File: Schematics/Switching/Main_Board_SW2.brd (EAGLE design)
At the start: 99.9 x 80 mm, 85 parts, among them IC3 SWITCHER, IC4 SWITCHER, Q1 32.768kHz, X1 MINI-USB-SHIELD-UX60-MB-5ST, X2 RJ45

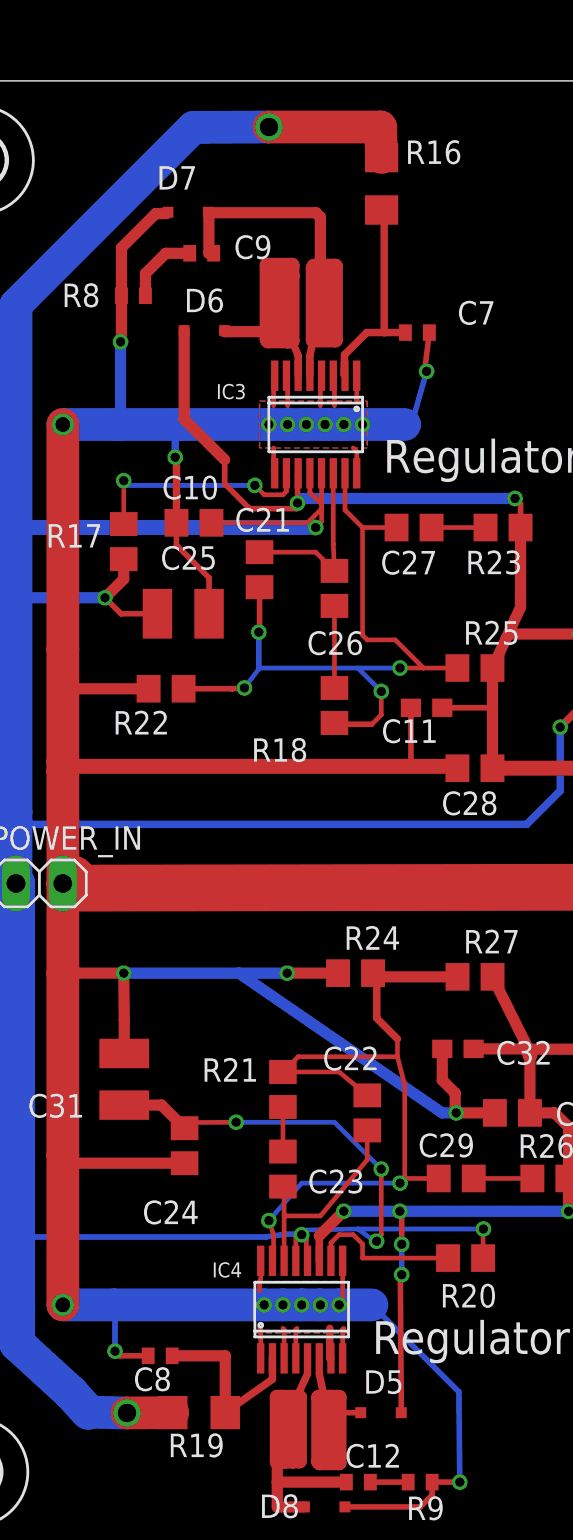
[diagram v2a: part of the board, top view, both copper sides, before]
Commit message: PCB Verified. Add Battery Sense
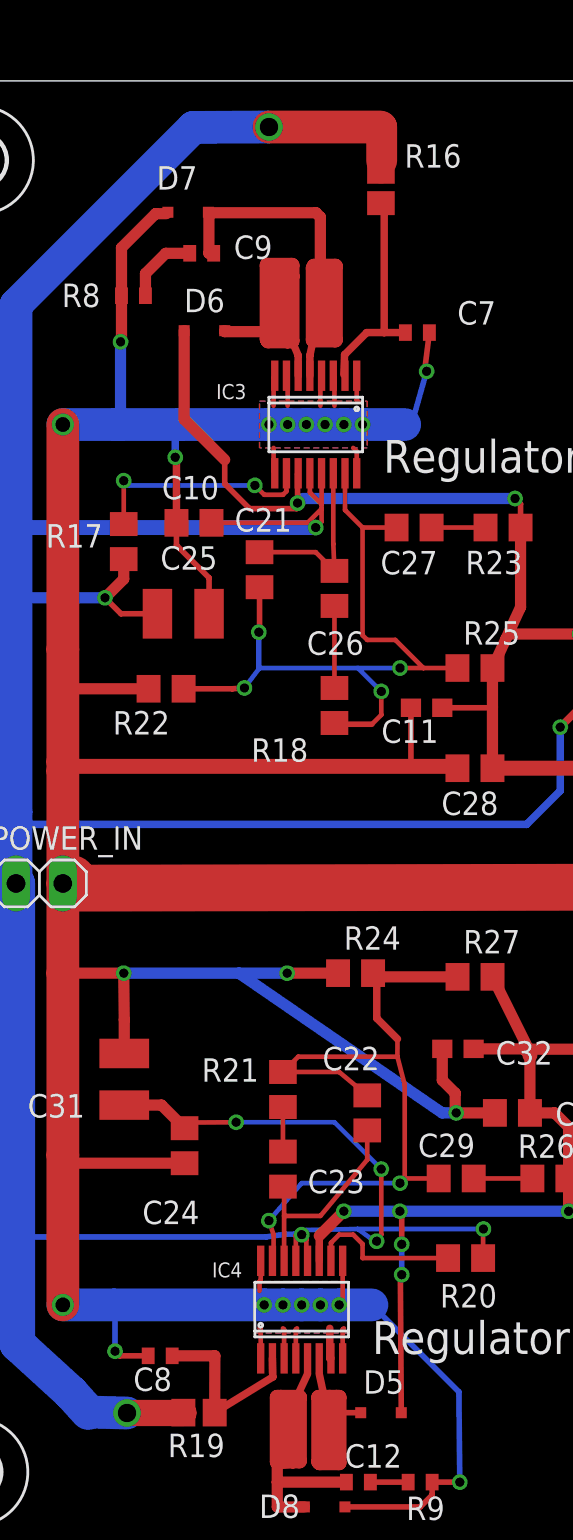
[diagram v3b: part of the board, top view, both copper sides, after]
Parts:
- R16, R19: device resistor:R1206 -> resistor:R0805
- moved R16 0.20 mm to (26.3, 74.2)
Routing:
- net V+: track 236.1 -> 237.5 mm
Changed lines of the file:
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@@
 <setting verticaltext="up"/>
 </settings>
-<grid distance="0.025" unitdist="mm" unit="mm" style="lines" multiple="1" display="yes" altdistance="0.025" altunitdist="mm" altunit="mm"/>
+<grid distance="0.0125" unitdist="mm" unit="mm" style="lines" multiple="1" display="yes" altdistance="0.0125" altunitdist="mm" altunit="mm"/>
 <layers>
 <layer number="1" name="Top" color="4" fill="1" visible="yes" active="yes"/>
@@
 <layer number="25" name="tNames" color="7" fill="1" visible="yes" active="yes"/>
 <layer number="26" name="bNames" color="7" fill="1" visible="yes" active="yes"/>
-<layer number="27" name="tValues" color="7" fill="1" visible="yes" active="yes"/>
-<layer number="28" name="bValues" color="7" fill="1" visible="yes" active="yes"/>
+<layer number="27" name="tValues" color="7" fill="1" visible="no" active="yes"/>
+<layer number="28" name="bValues" color="7" fill="1" visible="no" active="yes"/>
 <layer number="29" name="tStop" color="7" fill="3" visible="yes" active="yes"/>
 <layer number="30" name="bStop" color="7" fill="6" visible="yes" active="yes"/>
@@
 <attribute name="VALUE" x="32.0085" y="62.2785" size="0.8128" layer="27" font="vector" rot="R180"/>
 </element>
-<element name="R16" library="resistor" package="R1206" value="499K" x="26.36" y="74.372" smashed="yes" rot="R90">
-<attribute name="NAME" x="30.725" y="76.717" size="1.27" layer="25" rot="R180"/>
-<attribute name="VALUE" x="31.575" y="75.323" size="1.27" layer="27" rot="R180"/>
+<element name="R16" library="resistor" package="R0805" value="499K" x="26.3225" y="74.172" smashed="yes" rot="R90">
+<attribute name="NAME" x="30.6875" y="76.517" size="1.27" layer="25" rot="R180"/>
+<attribute name="VALUE" x="31.5375" y="75.123" size="1.27" layer="27" rot="R180"/>
 </element>
 <element name="R17" library="rcl" package="R0805" value="10k" x="12.372" y="54.964" smashed="yes" rot="R270">
@@
 <attribute name="VALUE" x="24.8815" y="15.5305" size="0.8128" layer="27" font="vector" rot="R270"/>
 </element>
-<element name="R19" library="resistor" package="R1206" value="499k" x="16.456" y="7.72" smashed="yes" rot="R180">
+<element name="R19" library="resistor" package="R0805" value="499k" x="16.456" y="7.72" smashed="yes" rot="R180">
 <attribute name="NAME" x="17.853" y="6.577" size="1.27" layer="25" rot="R180"/>
 <attribute name="VALUE" x="17.853" y="10.133" size="1.27" layer="27" rot="R180"/>
@@
 <wire x1="6.6" y1="11.45" x2="9.5" y2="8.8" width="1.9304" layer="16"/>
 <wire x1="6.53" y1="67.808" x2="16.15" y2="77.428" width="1.778" layer="16"/>
-<wire x1="26.3" y1="77.45" x2="26.36" y2="75.794" width="1.778" layer="1"/>
 <via x="12.55" y="7.7" extent="1-16" drill="1"/>
-<wire x1="15.034" y1="7.72" x2="12.55" y2="7.7" width="1.778" layer="1"/>
 <wire x1="12.55" y1="7.7" x2="10.45" y2="7.75" width="1.778" layer="16"/>
 <wire x1="16.15" y1="77.428" x2="20.25" y2="77.45" width="1.778" layer="16"/>
@@
 <wire x1="34.225" y1="39.625" x2="6.63" y2="39.625" width="0.4064" layer="16"/>
 <wire x1="6.63" y1="39.625" x2="6.53" y2="39.725" width="0.4064" layer="16"/>
+<wire x1="26.3" y1="77.45" x2="26.3625" y2="77.45" width="1.6764" layer="1"/>
+<wire x1="26.3625" y1="77.45" x2="26.3625" y2="75.6125" width="1.6764" layer="1"/>
+<wire x1="26.3625" y1="75.6125" x2="26.3225" y2="75.6125" width="1.27" layer="1"/>
+<wire x1="26.3225" y1="75.6125" x2="26.3225" y2="75.022" width="1.27" layer="1"/>
+<wire x1="12.55" y1="7.7" x2="15.606" y2="7.7" width="1.4224" layer="1"/>
+<wire x1="15.606" y1="7.7" x2="15.606" y2="7.72" width="1.4224" layer="1"/>
 </signal>
 <signal name="N$13">
@@
 <wire x1="25.55" y1="66.3" x2="26.5" y2="66.3" width="0.4064" layer="1"/>
 <wire x1="26.5" y1="66.3" x2="27.65" y2="66.3" width="0.4064" layer="1"/>
-<wire x1="26.36" y1="72.95" x2="26.5" y2="72.81" width="0.4064" layer="1"/>
+<wire x1="26.3225" y1="73.322" x2="26.5" y2="72.81" width="0.4064" layer="1"/>
 <wire x1="26.5" y1="72.81" x2="26.5" y2="66.3" width="0.4064" layer="1"/>
 </signal>
@@
 <contactref element="R19" pad="1"/>
 <contactref element="C8" pad="1"/>
-<wire x1="15" y1="10.8" x2="17.878" y2="10.8" width="0.6096" layer="1"/>
-<wire x1="17.878" y1="10.8" x2="17.878" y2="7.72" width="0.6096" layer="1"/>
-<wire x1="20.4365" y1="10.6622" x2="20.4365" y2="9.5285" width="0.4064" layer="1"/>
-<wire x1="20.4365" y1="9.5285" x2="17.878" y2="7.72" width="0.4064" layer="1"/>
+<wire x1="15" y1="10.8" x2="17.3155" y2="10.8" width="0.6096" layer="1"/>
+<wire x1="17.3155" y1="10.8" x2="17.306" y2="7.72" width="0.6096" layer="1"/>
+<wire x1="20.4365" y1="10.6622" x2="20.4615" y2="9.6535" width="0.4064" layer="1"/>
+<wire x1="20.4615" y1="9.6535" x2="17.306" y2="7.72" width="0.4064" layer="1"/>
 </signal>
 <signal name="N$33">

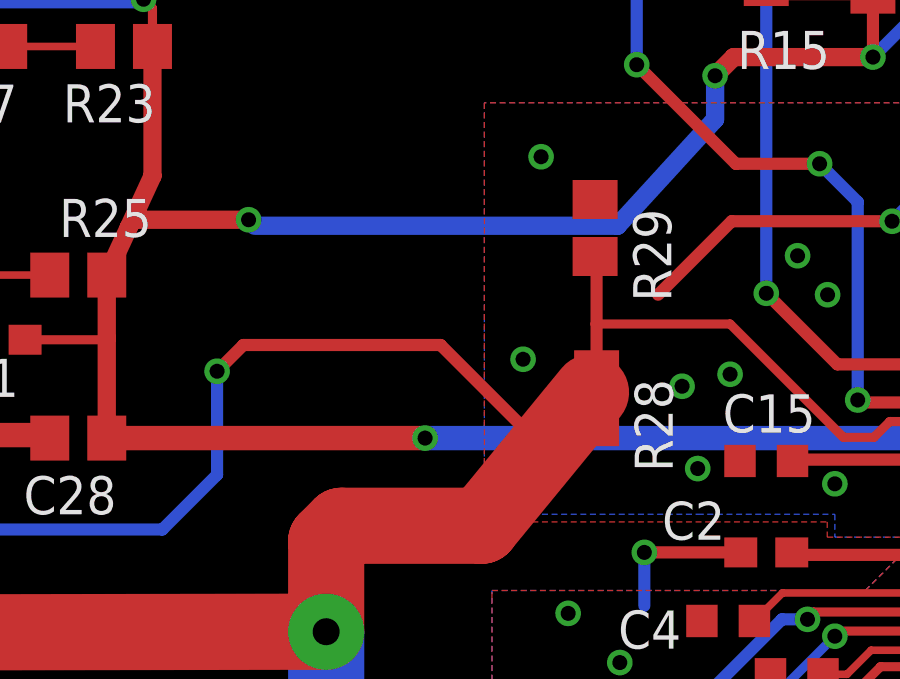
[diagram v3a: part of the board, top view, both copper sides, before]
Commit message: Batter Sense
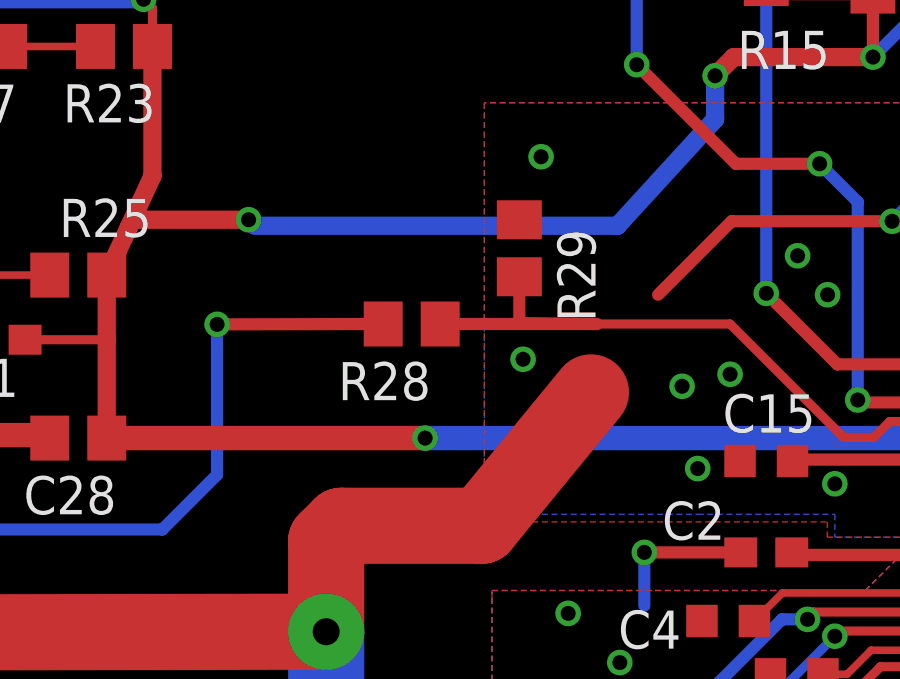
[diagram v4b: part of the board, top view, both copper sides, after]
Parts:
- moved R28 6.64 mm to (42.5, 46.5), turned to 180 degrees
- moved R29 2.61 mm to (46.1, 49.0)
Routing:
- net V+: track 237.5 -> 230.5 mm
- net N$22: track 16.5 -> 22.1 mm
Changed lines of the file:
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@@
 <element name="H3" library="holes" package="2,8" value="MOUNT-HOLE2.8" x="95.6" y="75.85"/>
 <element name="H4" library="holes" package="2,8" value="MOUNT-HOLE2.8" x="4.55" y="75.65"/>
-<element name="R28" library="rcl" package="R0805" value="5.6k" x="48.7" y="44" rot="R270"/>
-<element name="R29" library="rcl" package="R0805" value="5.6k" x="48.65" y="49.675" rot="R270"/>
+<element name="R28" library="rcl" package="R0805" value="5.6k" x="42.5375" y="46.475" rot="R180"/>
+<element name="R29" library="rcl" package="R0805" value="5.6k" x="46.125" y="49" rot="R270"/>
 </elements>
 <signals>
@@
 <wire x1="12.2" y1="61.564" x2="11.95" y2="61.314" width="0.6096" layer="16"/>
 <contactref element="R29" pad="1"/>
-<wire x1="61.214" y1="40.386" x2="61.42355" y2="38.14445" width="0" layer="19" extent="1-1"/>
 </signal>
 <signal name="N$11">
@@
 <wire x1="20.25" y1="77.45" x2="26.3" y2="77.45" width="1.778" layer="1"/>
 <contactref element="R28" pad="2"/>
-<wire x1="48.7" y1="43.05" x2="46.225" y2="43.05" width="0.4064" layer="1"/>
-<wire x1="46.225" y1="43.05" x2="43.5" y2="45.775" width="0.4064" layer="1"/>
-<wire x1="43.5" y1="45.775" x2="36.925" y2="45.775" width="0.4064" layer="1"/>
-<wire x1="36.925" y1="45.775" x2="36.05" y2="44.9" width="0.4064" layer="1"/>
 <wire x1="7.005" y1="39.825" x2="6.53" y2="40.3" width="0.4064" layer="16"/>
-<via x="36.05" y="44.9" extent="1-16" drill="0.5" diameter="0.254" shape="octagon"/>
-<wire x1="36.05" y1="44.9" x2="36.05" y2="41.45" width="0.4064" layer="16"/>
+<via x="36.05" y="46.4625" extent="1-16" drill="0.5" diameter="0.254" shape="octagon"/>
+<wire x1="36.05" y1="46.4625" x2="36.05" y2="41.45" width="0.4064" layer="16"/>
 <wire x1="36.05" y1="41.45" x2="34.225" y2="39.625" width="0.4064" layer="16"/>
 <wire x1="34.225" y1="39.625" x2="6.63" y2="39.625" width="0.4064" layer="16"/>
@@
 <wire x1="12.55" y1="7.7" x2="15.606" y2="7.7" width="1.4224" layer="1"/>
 <wire x1="15.606" y1="7.7" x2="15.606" y2="7.72" width="1.4224" layer="1"/>
+<wire x1="36.05" y1="46.4625" x2="41.5875" y2="46.475" width="0.4064" layer="1"/>
 </signal>
 <signal name="N$13">
@@
 <contactref element="R29" pad="2"/>
 <contactref element="R28" pad="1"/>
-<wire x1="48.7" y1="44.95" x2="48.7" y2="46.475" width="0.4064" layer="1"/>
-<wire x1="48.7" y1="46.475" x2="48.7" y2="48.675" width="0.4064" layer="1"/>
-<wire x1="48.7" y1="48.675" x2="48.65" y2="48.725" width="0.4064" layer="1"/>
+<wire x1="43.4875" y1="46.475" x2="48.7" y2="46.475" width="0.4064" layer="1"/>
+<wire x1="48.7" y1="46.475" x2="46.125" y2="46.5" width="0.4064" layer="1"/>
+<wire x1="46.125" y1="46.5" x2="46.125" y2="48.05" width="0.4064" layer="1"/>
 <contactref element="U$1" pad="P$44"/>
 <wire x1="59.65063125" y1="43.22445" x2="58.47445" y2="43.22445" width="0.3048" layer="1"/>

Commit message: Last layout sync of night
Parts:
- L1: value 4.7uH -> 3.3uH
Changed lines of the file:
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@@
 <?xml version="1.0" encoding="utf-8"?>
 <!DOCTYPE eagle SYSTEM "eagle.dtd">
-<eagle version="6.3">
+<eagle version="6.4">
 <drawing>
 <settings>
@@
 <layer number="26" name="bNames" color="7" fill="1" visible="yes" active="yes"/>
 <layer number="27" name="tValues" color="7" fill="1" visible="no" active="yes"/>
-<layer number="28" name="bValues" color="7" fill="1" visible="no" active="yes"/>
-<layer number="29" name="tStop" color="7" fill="3" visible="yes" active="yes"/>
-<layer number="30" name="bStop" color="7" fill="6" visible="yes" active="yes"/>
-<layer number="31" name="tCream" color="7" fill="4" visible="yes" active="yes"/>
-<layer number="32" name="bCream" color="7" fill="5" visible="yes" active="yes"/>
-<layer number="33" name="tFinish" color="6" fill="3" visible="yes" active="yes"/>
-<layer number="34" name="bFinish" color="6" fill="6" visible="yes" active="yes"/>
-<layer number="35" name="tGlue" color="7" fill="4" visible="yes" active="yes"/>
-<layer number="36" name="bGlue" color="7" fill="5" visible="yes" active="yes"/>
-<layer number="37" name="tTest" color="7" fill="1" visible="yes" active="yes"/>
-<layer number="38" name="bTest" color="7" fill="1" visible="yes" active="yes"/>
+<layer number="28" name="bValues" color="7" fill="1" visible="yes" active="yes"/>
+<layer number="29" name="tStop" color="7" fill="3" visible="no" active="yes"/>
+<layer number="30" name="bStop" color="7" fill="6" visible="no" active="yes"/>
+<layer number="31" name="tCream" color="7" fill="4" visible="no" active="yes"/>
+<layer number="32" name="bCream" color="7" fill="5" visible="no" active="yes"/>
+<layer number="33" name="tFinish" color="6" fill="3" visible="no" active="yes"/>
+<layer number="34" name="bFinish" color="6" fill="6" visible="no" active="yes"/>
+<layer number="35" name="tGlue" color="7" fill="4" visible="no" active="yes"/>
+<layer number="36" name="bGlue" color="7" fill="5" visible="no" active="yes"/>
+<layer number="37" name="tTest" color="7" fill="1" visible="no" active="yes"/>
+<layer number="38" name="bTest" color="7" fill="1" visible="no" active="yes"/>
 <layer number="39" name="tKeepout" color="4" fill="11" visible="yes" active="yes"/>
 <layer number="40" name="bKeepout" color="1" fill="11" visible="yes" active="yes"/>
@@
 <layer number="42" name="bRestrict" color="1" fill="10" visible="yes" active="yes"/>
 <layer number="43" name="vRestrict" color="2" fill="10" visible="yes" active="yes"/>
-<layer number="44" name="Drills" color="7" fill="1" visible="yes" active="yes"/>
-<layer number="45" name="Holes" color="7" fill="1" visible="yes" active="yes"/>
-<layer number="46" name="Milling" color="3" fill="1" visible="yes" active="yes"/>
-<layer number="47" name="Measures" color="7" fill="1" visible="yes" active="yes"/>
+<layer number="44" name="Drills" color="7" fill="1" visible="no" active="yes"/>
+<layer number="45" name="Holes" color="7" fill="1" visible="no" active="yes"/>
+<layer number="46" name="Milling" color="3" fill="1" visible="no" active="yes"/>
+<layer number="47" name="Measures" color="7" fill="1" visible="no" active="yes"/>
 <layer number="48" name="Document" color="7" fill="1" visible="yes" active="yes"/>
 <layer number="49" name="Reference" color="7" fill="1" visible="yes" active="yes"/>
 <layer number="50" name="dxf" color="7" fill="1" visible="no" active="no"/>
 <layer number="51" name="tDocu" color="7" fill="1" visible="yes" active="yes"/>
-<layer number="52" name="bDocu" color="7" fill="1" visible="yes" active="yes"/>
+<layer number="52" name="bDocu" color="7" fill="1" visible="no" active="yes"/>
 <layer number="53" name="tGND_GNDA" color="7" fill="1" visible="no" active="no"/>
 <layer number="54" name="bGND_GNDA" color="7" fill="1" visible="no" active="no"/>
@@
 <layer number="99" name="SpiceOrder" color="5" fill="1" visible="no" active="no"/>
 <layer number="100" name="Mechanical" color="7" fill="1" visible="no" active="no"/>
-<layer number="101" name="Gehäuse" color="7" fill="1" visible="yes" active="yes"/>
-<layer number="102" name="Mittellin" color="7" fill="1" visible="yes" active="yes"/>
-<layer number="103" name="Stiffner" color="7" fill="1" visible="yes" active="yes"/>
-<layer number="104" name="Name" color="7" fill="1" visible="yes" active="yes"/>
+<layer number="101" name="Gehäuse" color="7" fill="1" visible="no" active="yes"/>
+<layer number="102" name="Mittellin" color="7" fill="1" visible="no" active="yes"/>
+<layer number="103" name="Stiffner" color="7" fill="1" visible="no" active="yes"/>
+<layer number="104" name="Name" color="7" fill="1" visible="no" active="yes"/>
 <layer number="105" name="Beschreib" color="9" fill="1" visible="no" active="no"/>
 <layer number="106" name="BGA-Top" color="4" fill="1" visible="no" active="no"/>
@@
 <layer number="114" name="Route14" color="7" fill="1" visible="no" active="no"/>
 <layer number="115" name="Route15" color="7" fill="1" visible="no" active="no"/>
-<layer number="116" name="Patch_BOT" color="7" fill="1" visible="yes" active="yes"/>
+<layer number="116" name="Patch_BOT" color="7" fill="1" visible="no" active="yes"/>
 <layer number="117" name="mPads" color="7" fill="1" visible="no" active="no"/>
 <layer number="118" name="mVias" color="7" fill="1" visible="no" active="no"/>
@@
 <layer number="148" name="mDocument" color="7" fill="1" visible="no" active="no"/>
 <layer number="149" name="mReference" color="7" fill="1" visible="no" active="no"/>
-<layer number="150" name="Notes" color="7" fill="1" visible="yes" active="yes"/>
+<layer number="150" name="Notes" color="7" fill="1" visible="no" active="yes"/>
 <layer number="151" name="HeatSink" color="14" fill="1" visible="no" active="no"/>
 <layer number="152" name="mbDocu" color="7" fill="1" visible="no" active="no"/>
@@
 <layer number="195" name="mNames" color="7" fill="1" visible="no" active="no"/>
 <layer number="196" name="mValues" color="7" fill="1" visible="no" active="no"/>
-<layer number="199" name="EXTD_ERC" color="7" fill="1" visible="yes" active="yes"/>
+<layer number="199" name="EXTD_ERC" color="7" fill="1" visible="no" active="yes"/>
 <layer number="200" name="200bmp" color="1" fill="10" visible="no" active="no"/>
 <layer number="201" name="201bmp" color="2" fill="1" visible="no" active="no"/>
 <layer number="202" name="202bmp" color="3" fill="1" visible="no" active="no"/>
-<layer number="216" name="SMD16" color="7" fill="1" visible="yes" active="yes"/>
+<layer number="216" name="SMD16" color="7" fill="1" visible="no" active="yes"/>
 <layer number="231" name="Eagle3D_PG1" color="14" fill="1" visible="yes" active="yes"/>
 <layer number="232" name="Eagle3D_PG2" color="14" fill="2" visible="yes" active="yes"/>
@@
 </polygon>
 <text x="91.9" y="34.1" size="1.778" layer="25">USB</text>
-<text x="42.35" y="70.3" size="1.778" layer="25">Ethernet</text>
-<text x="52.55" y="27.8" size="1.778" layer="25">Microcontroller</text>
+<text x="44.8875" y="62.0875" size="1.778" layer="25">Ethernet</text>
+<text x="46.725" y="26.825" size="1.778" layer="25">Microcontroller</text>
 <text x="68" y="14.05" size="1.778" layer="25">Programmer</text>
 <text x="26.45" y="58.7" size="1.778" layer="25">Regulator 5V</text>
@@
 <attribute name="VALUE" x="8.301" y="52.932" size="1.27" layer="27"/>
 </element>
-<element name="L1" library="Inductor" package="SHEILDED_COIL" value="4.7uH" x="23.29" y="66.61" smashed="yes">
-<attribute name="VALUE" x="20.965" y="65.86" size="0.227" layer="48"/>
-<attribute name="NAME" x="20.75" y="69.375" size="0.227" layer="48"/>
+<element name="L1" library="Inductor" package="SHEILDED_COIL" value="3.3uH" x="23.29" y="66.61" smashed="yes">
+<attribute name="VALUE" x="20.965" y="65.86" size="0.227" layer="27"/>
+<attribute name="NAME" x="20.75" y="69.375" size="1.27" layer="48"/>
 </element>
 <element name="D6" library="diode" package="SOD323-R" value="" x="16.75" y="66.404" smashed="yes">
@@
 </element>
 <element name="L2" library="Inductor" package="SHEILDED_COIL" value="4.7uH" x="21.212" y="7.882" smashed="yes" rot="R180">
-<attribute name="VALUE" x="23.537" y="8.632" size="0.227" layer="48" rot="R180"/>
-<attribute name="NAME" x="23.752" y="5.117" size="0.227" layer="48" rot="R180"/>
+<attribute name="VALUE" x="23.537" y="8.632" size="0.227" layer="27" rot="R180"/>
+<attribute name="NAME" x="22.727" y="4.867" size="0.8128" layer="25" rot="R180"/>
 </element>
 <element name="D5" library="diode" package="SOD323-R" value="" x="26.326" y="7.716" smashed="yes" rot="R180">
